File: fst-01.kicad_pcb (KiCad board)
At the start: 2 copper layers, 26.5 x 13.1 mm, 24 parts, among them J1 USB_A, K1 CONN_3, K2 CONN_2, K3 CONN_2, U1 STM32F103TB, U2 LP2985-33DBVR, U3 NUF2221W1, U4 SST25VF032B, X1 12MHz

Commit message: update PCB
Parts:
- C1, C11, C2, C3, C4, C5, C6, C7, C9: footprint c_0402 -> FST:c_0402
- C10, C8: footprint c_0603 -> FST:c_0603
- R1: footprint r_0402 -> FST:r_0402
- X1: footprint ABM8G -> FST:ABM8G

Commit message: fix U1 and U2
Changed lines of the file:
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@@
     (last_trace_width 0.20066)
     (trace_clearance 0.20066)
-    (zone_clearance 0.20066)
-    (zone_45_only no)
+    (zone_clearance 0.508)
+    (zone_45_only yes)
     (trace_min 0.20066)
     (segment_width 0.381)
@@
     (aux_axis_origin 127 98.9965)
     (grid_origin 127 98.9965)
-    (visible_elements 7FFFFFFF)
+    (visible_elements 7FFFFF7F)
     (pcbplotparams
       (layerselection 0x010f0_80000001)
@@
       (effects (font (size 0.8001 0.8001) (thickness 0.1524)))
     )
-    (fp_text value LP2985-33DBVR (at -0.0127 0 90) (layer F.SilkS)
+    (fp_text value LP2985-33DBVR (at -0.0127 0 90) (layer F.SilkS) hide
       (effects (font (size 0.254 0.254) (thickness 0.0254)))
     )
@@
     (polygon
       (pts
-        (xy 125.01626 105.6767) (xy 125.0188 100.5713) (xy 126.0348 100.5713) (xy 126.0348 95.5421) (xy 126.3396 95.5421)
-        (xy 126.3396 92.3925) (xy 105.30586 92.37726) (xy 105.30586 105.6767)
+        (xy 126.3396 92.3925) (xy 126.3396 95.5421) (xy 126.0348 95.5421) (xy 126.0348 100.5713) (xy 125.0188 100.5713)
+        (xy 125.01626 105.6767) (xy 105.30586 105.6767) (xy 105.30586 92.37726) (xy 126.3396 92.3925)
       )
     )
@@
       )
     )
+  )
+  (zone (net 0) (net_name "") (layer Front) (hatch edge 0.508)
+    (connect_pads (clearance 0.508))
+    (min_thickness 0.254)
+    (keepout (tracks allowed) (vias allowed) (copperpour not_allowed))
+    (fill (arc_segments 16) (thermal_gap 0.508) (thermal_bridge_width 0.508))
+    (polygon
+      (pts
+        (xy 116.459 96.7105) (xy 119.634 96.7105) (xy 119.634 100.2665) (xy 116.459 100.2665)
+      )
+    )

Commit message: Add WEEE-logo
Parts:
- added REF***: WEEE-Logo_4.2x6mm_SilkScreen, FST:WEEE-Logo_4.2x6mm_SilkScreen, B.Cu at (118.2, 100.5)

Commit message: added & improved FST-01R design
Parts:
- removed CE_mark: Symbol_CE_SilkScreen_5mm, Symbols:Symbol_CE_SilkScreen_5mm
- removed FST-LOGO: VAL**, FST-LOGO
- removed REF***: WEEE-Logo_4.2x6mm_SilkScreen, FST:WEEE-Logo_4.2x6mm_SilkScreen
- K1: value CONN_3 -> K1; footprint SIL-3-2 -> FST:SIL-3-2
- K2: value CONN_2 -> K2; footprint SIL-2-0 -> FST:SIL-2-0
- K3: value CONN_2 -> K3; footprint SIL-2-2 -> FST:SIL-2-2
- U1: value STM32F103TB -> GD32F103TB
- U3: footprint SOT363 -> FST:SOT363
- U4: footprint WSON8 -> FST:WSON8
- turned K3 to 180 degrees
- turned K2 to 90 degrees
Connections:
- K2 pad 1: +3V3 -> GND
- K2 pad 2: GND -> +3V3
- K3 pad 1: /PA2 -> /PA3
- K3 pad 2: /PA3 -> /PA2
- U1 pad 16: (no net) -> Net-(U1-Pad16)
- U1 pad 20: (no net) -> Net-(U1-Pad20)
- U1 pad 21: (no net) -> Net-(U1-Pad21)
- U1 pad 22: (no net) -> Net-(U1-Pad22)
- U1 pad 29: (no net) -> Net-(U1-Pad29)
- U1 pad 30: (no net) -> Net-(U1-Pad30)
- U1 pad 31: (no net) -> Net-(U1-Pad31)
- U1 pad 32: (no net) -> Net-(U1-Pad32)
- U1 pad 33: (no net) -> Net-(U1-Pad33)
- U1 pad 34: (no net) -> Net-(U1-Pad34)
- U1 pad 7: (no net) -> Net-(U1-Pad7)
- U1 pad 8: (no net) -> Net-(U1-Pad8)
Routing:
- net GND: vias 6 -> 8
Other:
- board size 26.5 x 13.1 mm -> 28.9 x 13.1 mm

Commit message: FST-01R rev1.1
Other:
- rule pad_to_mask_clearance: 0.1524 -> 0

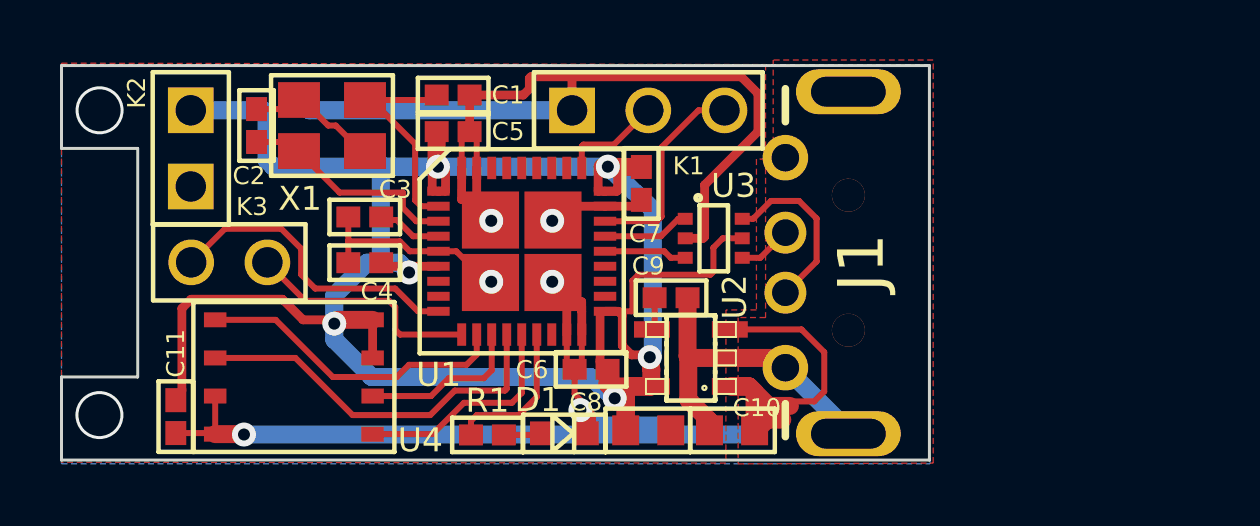
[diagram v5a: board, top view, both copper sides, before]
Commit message: rev1.2; changed PA3 pad to NRST for easier debugging
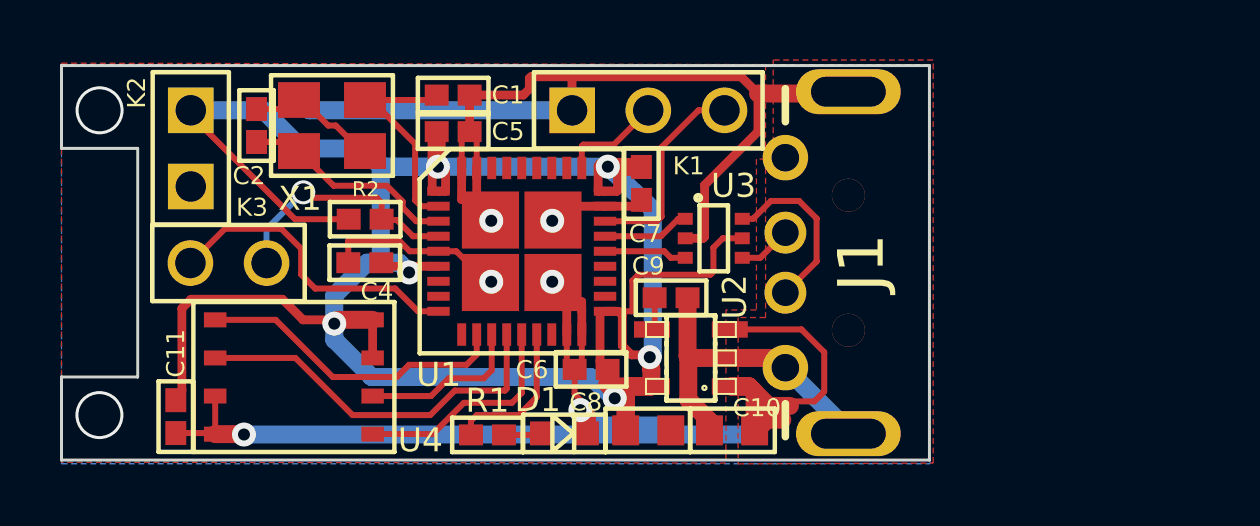
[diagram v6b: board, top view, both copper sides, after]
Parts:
- removed C3: 0.1uF, FST:c_0402
- added R2: 510, FST:r_0402, F.Cu at (113.0, 97.5)
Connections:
- K3 pad 1: /PA3 -> /NRST
- U1 pad 10: /PA3 -> Net-(U1-Pad10)
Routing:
- net /PA3: track 7.92 -> 0.00 mm
- net /NRST: track 2.17 -> 8.34 mm, vias 0 -> 1
- net +3V3: track 87.6 -> 93.6 mm
- net GND: track 94.2 -> 96.5 mm
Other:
- board text added: "FST-01R"
- board text removed: "FST-01G"

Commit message: added boot0 support: both pin and jumper pad
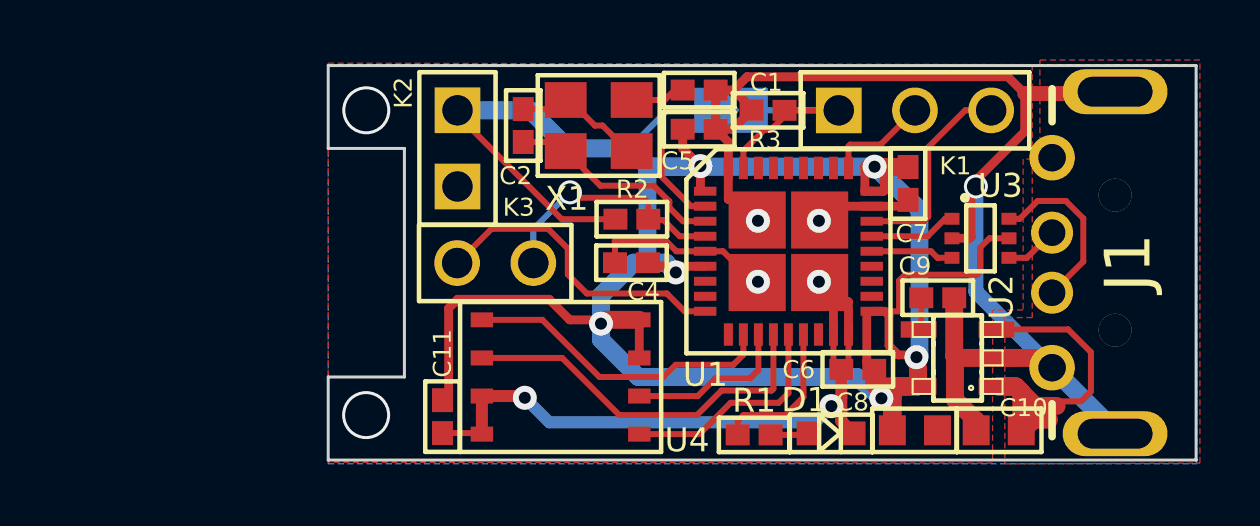
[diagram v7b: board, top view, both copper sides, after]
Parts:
- added JP1: Jumper_2_Open, Jumper:SolderJumper-2_P1.3mm_Open_TrianglePad1.0x1.5mm, B.Cu at (125.2, 93.9)
- added R3: 510, FST:r_0402, F.Cu at (126.4, 93.9)
- moved C6 8.89 mm to (129.4, 102.6)
- moved C7 8.89 mm to (131.1, 96.4)
- moved C8 8.89 mm to (131.3, 104.6)
- moved C9 8.89 mm to (132.1, 100.2)
- moved C10 8.89 mm to (134.1, 104.6)
- moved C2 8.89 mm to (118.3, 94.4)
- moved C4 8.89 mm to (121.9, 99.0)
- moved D1 8.89 mm to (128.5, 104.7)
- moved K1 8.89 mm to (131.3, 93.9)
- moved K2 8.89 mm to (116.1, 95.2)
- moved K3 8.89 mm to (117.3, 99.0)
- moved R1 8.89 mm to (126.0, 104.7)
- moved R2 8.89 mm to (121.9, 97.5)
- moved U1 8.89 mm to (127.1, 98.6)
- moved U2 8.89 mm to (132.7, 102.2)
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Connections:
- K1 pad 1: GND -> /BOOT0
- U1 pad 35: GND -> /BOOT0
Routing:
- net GND: track 96.5 -> 84.1 mm, vias 8 -> 9
- net /BOOT0: track 0.00 -> 7.60 mm
- net +3V3: track 93.6 -> 94.8 mm
- net /OSC_IN: track 7.47 -> 6.58 mm
